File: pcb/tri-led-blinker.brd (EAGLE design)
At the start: 80 x 49 mm, 13 parts, among them J1 MICRO-USB-SMD(ZX62-B-5PA), K1 TS-1109

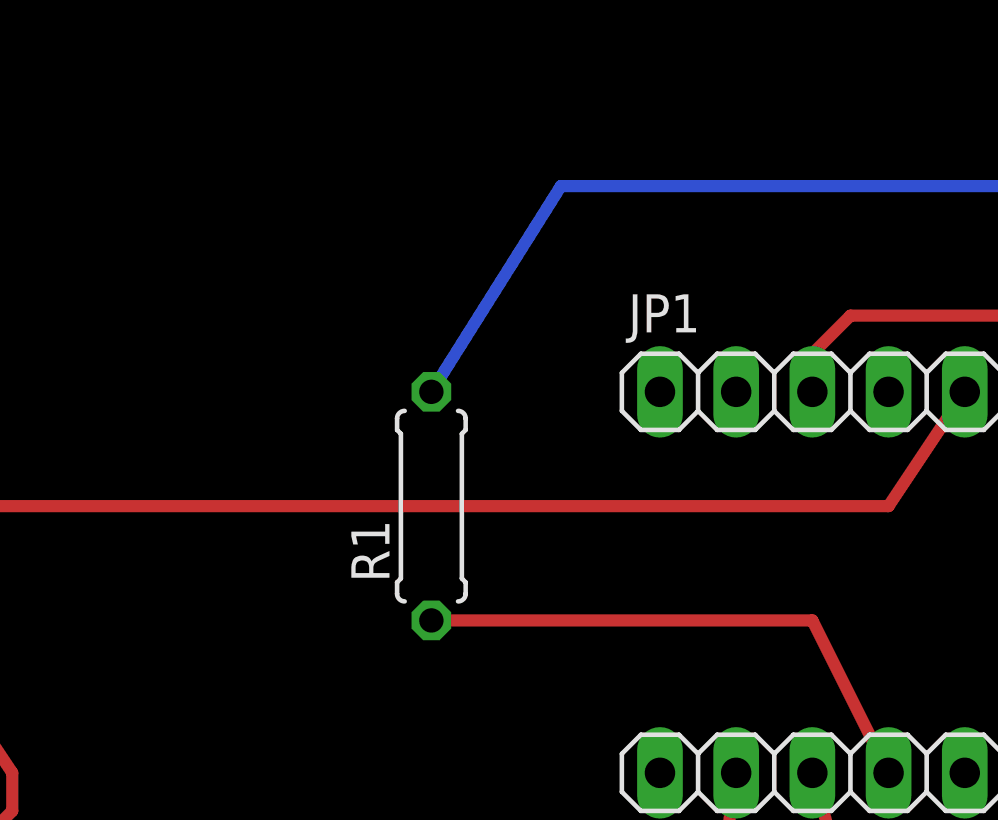
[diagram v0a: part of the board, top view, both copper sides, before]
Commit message: shift resistor r1 a bit to the left
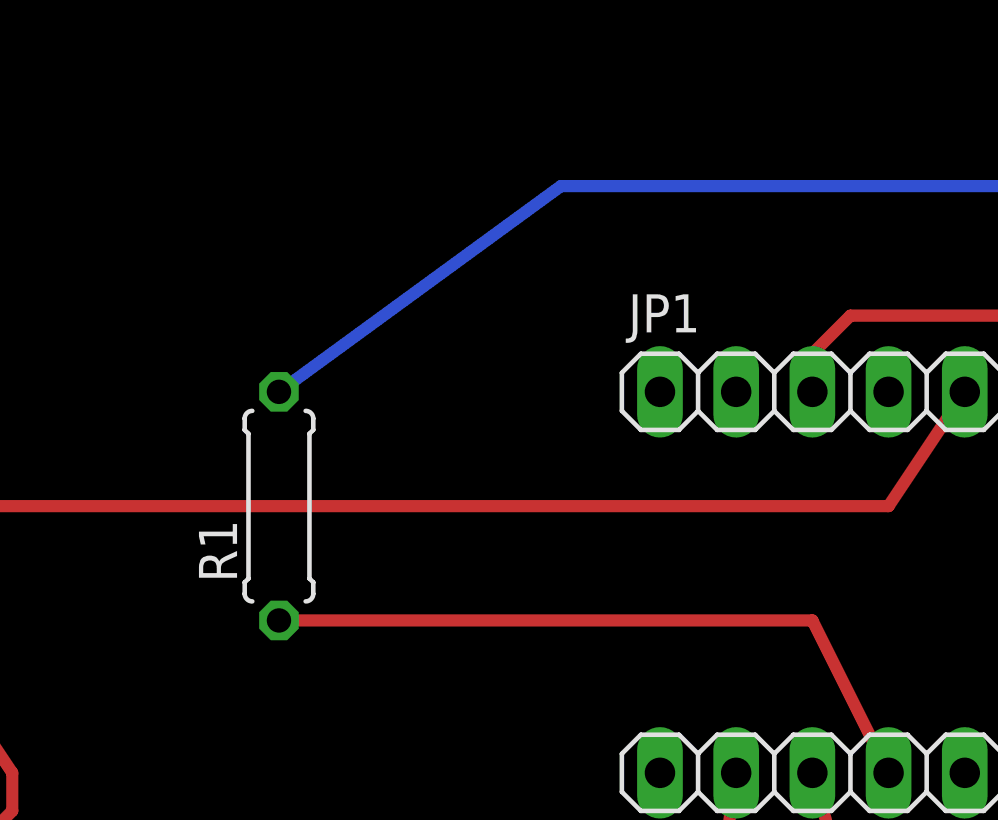
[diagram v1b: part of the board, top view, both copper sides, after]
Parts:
- moved R1 5.08 mm to (35.6, 27.9)
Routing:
- net N$8: track 18.4 -> 23.5 mm
- net N$1: track 26.6 -> 30.2 mm
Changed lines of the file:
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@@
 <layer number="23" name="tOrigins" color="15" fill="1" visible="yes" active="yes"/>
 <layer number="24" name="bOrigins" color="15" fill="1" visible="yes" active="yes"/>
-<layer number="25" name="tNames" color="7" fill="1" visible="no" active="yes"/>
-<layer number="26" name="bNames" color="7" fill="1" visible="no" active="yes"/>
+<layer number="25" name="tNames" color="7" fill="1" visible="yes" active="yes"/>
+<layer number="26" name="bNames" color="7" fill="1" visible="yes" active="yes"/>
 <layer number="27" name="tValues" color="7" fill="1" visible="no" active="yes"/>
 <layer number="28" name="bValues" color="7" fill="1" visible="no" active="yes"/>
@@
 <attribute name="VALUE" value="TS-1109" x="74.295" y="38.1" size="0.889" layer="27" ratio="11" rot="R90"/>
 </element>
-<element name="R1" library="resistor" package="0207/7" value="" x="40.64" y="27.94" rot="R90"/>
+<element name="R1" library="resistor" package="0207/7" value="" x="35.56" y="27.94" rot="R90"/>
 <element name="R2" library="resistor" package="0207/7" value="" x="59.69" y="10.16" smashed="yes">
 <attribute name="NAME" x="59.055" y="7.112" size="1.27" layer="25" ratio="10"/>
@@
 <contactref element="R1" pad="2"/>
 <contactref element="D1" pad="+"/>
-<wire x1="40.64" y1="31.75" x2="44.958" y2="38.608" width="0.4064" layer="16"/>
+<wire x1="35.56" y1="31.75" x2="44.958" y2="38.608" width="0.4064" layer="16"/>
 <wire x1="44.958" y1="38.608" x2="63.5" y2="38.608" width="0.4064" layer="16"/>
 </signal>
@@
 <contactref element="JP2" pad="4"/>
 <wire x1="55.88" y1="19.05" x2="53.34" y2="24.13" width="0.4064" layer="1"/>
-<wire x1="53.34" y1="24.13" x2="40.64" y2="24.13" width="0.4064" layer="1"/>
+<wire x1="53.34" y1="24.13" x2="35.56" y2="24.13" width="0.4064" layer="1"/>
 </signal>
 <signal name="N$9">
